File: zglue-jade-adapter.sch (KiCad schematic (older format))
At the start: 76 parts, among them J1 543630489, J2 543630489, U1 zGlue-Jade

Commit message: Update pinout and layout
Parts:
- removed TP28: TP_SMD1MM, antmicro-footprints:Testpoint_smd_1mm, symbol antmicroTestPoints:TP_SMD1MM
- added R29: R_0R_0402, antmicro-footprints:0402-res, symbol antmicroResistors0402:R_0R_0402
- added TP1: TP_SMD1MM, antmicro-footprints:Testpoint_smd_1mm, symbol antmicroTestPoints:TP_SMD1MM
- U1: symbol zglue-jade:zGlue-Jade -> zglue-jade-adapter-rescue:zGlue-Jade-zglue-jade
- renumbered TP1 to TP28
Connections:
- net labels added: PIO0, PIO13, PIO14
- net labels removed: PIO16, PIO17
- wire segments 277 -> 280
- no-connect marks 1 -> 14
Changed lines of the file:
@@
 	4200 4200 4800 4200
 Wire Wire Line
-	4200 4300 4800 4300
-Wire Wire Line
-	4200 4400 4800 4400
-Wire Wire Line
-	4200 4500 4800 4500
-Wire Wire Line
-	4200 4600 4800 4600
+	4200 4350 4800 4350
+Wire Wire Line
+	4200 4450 4800 4450
+Wire Wire Line
+	4200 4550 4800 4550
+Wire Wire Line
+	4200 4650 4800 4650
 Wire Wire Line
 	4200 4850 4800 4850
@@
 Text Label 4350 4200 0    50   ~ 0
 PROC_RST
-Text Label 4350 4300 0    50   ~ 0
+Text Label 1750 7050 0    50   ~ 0
 PROC_SI
-Text Label 4350 4400 0    50   ~ 0
+Text Label 1750 6950 0    50   ~ 0
 PROC_SO
-Text Label 4350 4500 0    50   ~ 0
+Text Label 1750 6750 0    50   ~ 0
 PROC_SCK
-Text Label 4350 4600 0    50   ~ 0
+Text Label 1750 6850 0    50   ~ 0
 PROC_SS
 Text Label 4350 4850 0    50   ~ 0
@@
 $EndComp
 $Comp
-L antmicroTestPoints:TP_SMD1MM TP1
+L antmicroTestPoints:TP_SMD1MM TP28
 U 1 1 5E08B0FD
 P 1650 5550
-F 0 "TP1" V 1650 5400 50  0000 C CNN
+F 0 "TP28" V 1650 5400 50  0000 C CNN
 F 1 "TP_SMD1MM" H 1650 5450 50  0001 C CNN
 F 2 "antmicro-footprints:Testpoint_smd_1mm" H 1850 5750 60  0001 L CNN
@@
 PIO15
 Wire Wire Line
-	2350 6950 1650 6950
+	2350 6950 1750 6950
 Wire Wire Line
 	2350 6750 1750 6750
 Wire Wire Line
 	2350 6850 1750 6850
-$Comp
-L antmicroTestPoints:TP_SMD1MM TP29
-U 1 1 5E0DD5A6
-P 1650 6850
-F 0 "TP29" V 1650 6700 50  0000 C CNN
-F 1 "TP_SMD1MM" H 1650 6750 50  0001 C CNN
-F 2 "antmicro-footprints:Testpoint_smd_1mm" H 1850 7050 60  0001 L CNN
-F 3 "" H 1850 7150 60  0001 L CNN
-	1    1650 6850
-	0    1    1    0
-$EndComp
-$Comp
-L antmicroTestPoints:TP_SMD1MM TP28
-U 1 1 5E0DD5AD
-P 1650 6750
-F 0 "TP28" V 1650 6600 50  0000 C CNN
-F 1 "TP_SMD1MM" H 1650 6650 50  0001 C CNN
-F 2 "antmicro-footprints:Testpoint_smd_1mm" H 1850 6950 60  0001 L CNN
-F 3 "" H 1850 7050 60  0001 L CNN
-	1    1650 6750
-	0    1    1    0
-$EndComp
-Text Label 1750 6850 0    50   ~ 0
-PIO17
-Text Label 1750 6750 0    50   ~ 0
-PIO16
-Wire Wire Line
-	2350 7050 1650 7050
-$Comp
-L zglue-jade:zGlue-Jade U1
+Text Label 1750 6550 0    50   ~ 0
+PIO14
+Text Label 1750 6450 0    50   ~ 0
+PIO13
+Wire Wire Line
+	2350 7050 1750 7050
+$Comp
+L zglue-jade-adapter-rescue:zGlue-Jade-zglue-jade U1
 U 1 1 5DB41B4F
 P 3200 3450
@@
 	0    1    1    0
 $EndComp
-Text Label 1750 6450 0    50   ~ 0
+Text Label 4350 4650 0    50   ~ 0
 PROC_INT
-Text Label 1750 6550 0    50   ~ 0
+Text Label 4350 4350 0    50   ~ 0
 CSI_INT
-Text Label 1650 6950 0    50   ~ 0
+Text Label 4350 4450 0    50   ~ 0
 LP_CSI_D1_OUT_P
-Text Label 1650 7050 0    50   ~ 0
+Text Label 4350 4550 0    50   ~ 0
 LP_CSI_D1_OUT_N
 Text Notes 6450 2600 0    50   ~ 0
 DNP
+NoConn ~ 8800 2550
+NoConn ~ 8800 2650
+NoConn ~ 8800 2850
+NoConn ~ 8800 2950
+NoConn ~ 9250 2950
+NoConn ~ 9250 3050
+NoConn ~ 12300 2250
+NoConn ~ 12300 2350
+NoConn ~ 12300 2550
+NoConn ~ 12300 2650
+NoConn ~ 12300 2850
+NoConn ~ 12300 2950
+NoConn ~ 12300 3150
+Wire Wire Line
+	2350 5150 1750 5150
+$Comp
+L antmicroTestPoints:TP_SMD1MM TP1
+U 1 1 5DF17D2C
+P 1650 5150
+F 0 "TP1" V 1650 5000 50  0000 C CNN
+F 1 "TP_SMD1MM" H 1650 5050 50  0001 C CNN
+F 2 "antmicro-footprints:Testpoint_smd_1mm" H 1850 5350 60  0001 L CNN
+F 3 "" H 1850 5450 60  0001 L CNN
+	1    1650 5150
+	0    1    1    0
+$EndComp
+Text Label 1750 5150 0    50   ~ 0
+PIO0
+Text Label 7900 4600 0    50   ~ 0
+PROC_RST
+$Comp
+L antmicroTestPoints:TP_SMD1MM TP29
+U 1 1 5DF566CE
+P 4900 4650
+F 0 "TP29" V 4900 4500 50  0000 C CNN
+F 1 "TP_SMD1MM" H 4900 4550 50  0001 C CNN
+F 2 "antmicro-footprints:Testpoint_smd_1mm" H 5100 4850 60  0001 L CNN
+F 3 "" H 5100 4950 60  0001 L CNN
+	1    4900 4650
+	0    -1   -1   0
+$EndComp
+$Comp
+L antmicroResistors0402:R_0R_0402 R29
+U 1 1 5DF56D0B
+P 8600 4600
+F 0 "R29" H 8800 4650 60  0000 C CNN
+F 1 "R_0R_0402" H 8600 4450 60  0001 C CNN
+F 2 "antmicro-footprints:0402-res" H 8800 4800 60  0001 L CNN
+F 3 "" H 8600 4600 50  0001 C CNN
+F 4 "PANASONIC" H 8800 5000 60  0001 L CNN "Manufacturer"
+F 5 "ERJ2GE0R00X" H 8800 4900 60  0001 L CNN "MPN"
+F 6 "0R" H 8950 4650 50  0000 C CNN "Val"
+	1    8600 4600
+	1    0    0    -1
+$EndComp
+Wire Wire Line
+	7900 4600 8450 4600
+Wire Wire Line
+	8750 4600 9700 4600
+Text Label 9100 4600 0    50   ~ 0
+E_PROC_RST
 $EndSCHEMATC

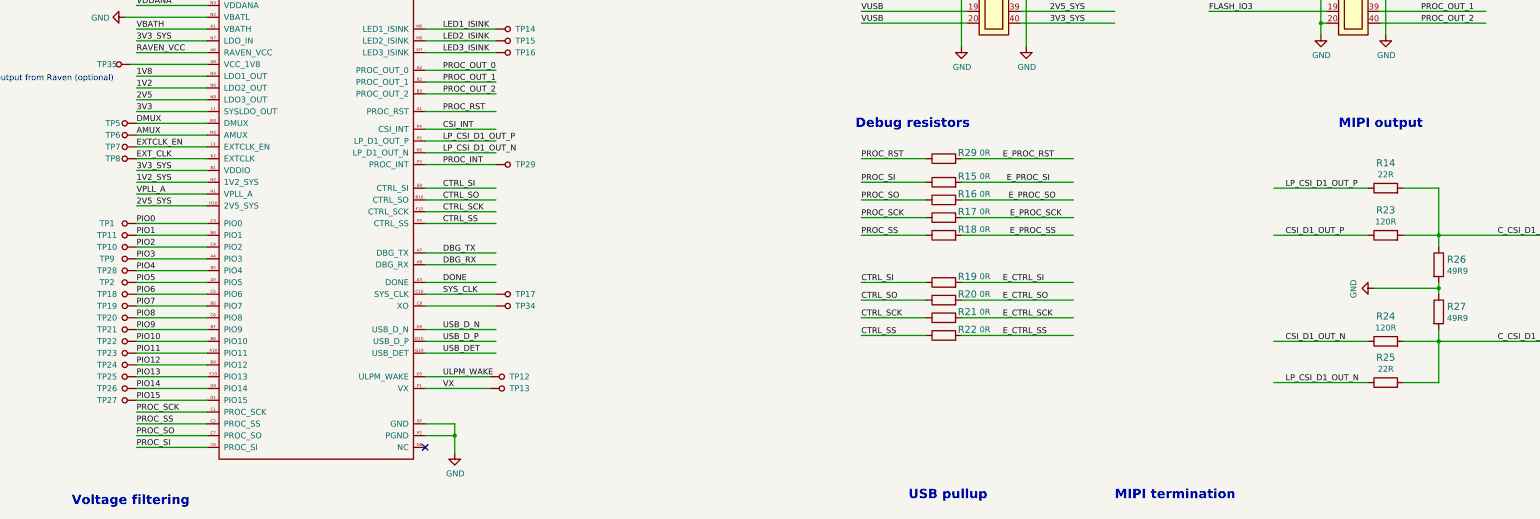
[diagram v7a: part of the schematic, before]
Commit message: Add resistors for choosing CSI_LP signals connection
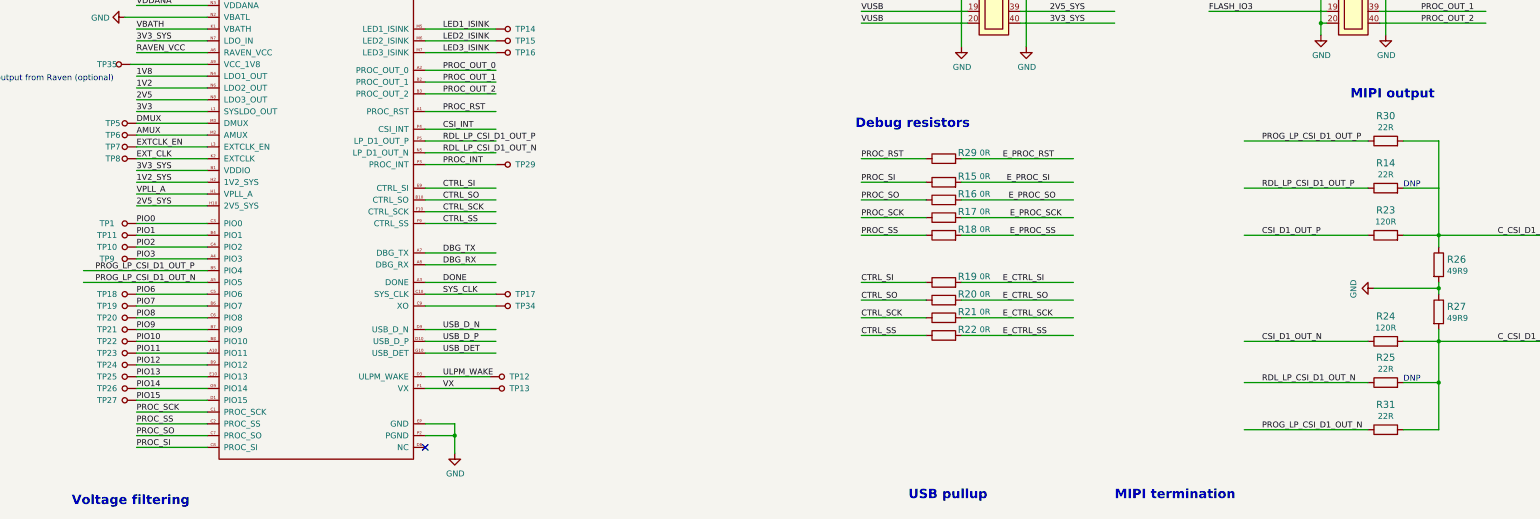
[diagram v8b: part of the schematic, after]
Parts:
- removed TP2, TP28: TP_SMD1MM, antmicro-footprints:Testpoint_smd_1mm, symbol antmicroTestPoints:TP_SMD1MM
- added R30, R31: R_22R_0402, antmicro-footprints:0402-res, symbol antmicroResistors0402:R_22R_0402
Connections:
- net labels added: PROG_LP_CSI_D1_OUT_N, PROG_LP_CSI_D1_OUT_P, RDL_LP_CSI_D1_OUT_N, RDL_LP_CSI_D1_OUT_P
- net labels removed: LP_CSI_D1_OUT_N, LP_CSI_D1_OUT_P, PIO4, PIO5
- wire segments 280 -> 286
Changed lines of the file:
@@
 	2350 5750 1750 5750
 Wire Wire Line
-	2350 5550 1750 5550
-Wire Wire Line
-	2350 5650 1750 5650
+	2350 5550 1300 5550
+Wire Wire Line
+	2350 5650 1300 5650
 $Comp
 L antmicroTestPoints:TP_SMD1MM TP18
@@
 	0    1    1    0
 $EndComp
-$Comp
-L antmicroTestPoints:TP_SMD1MM TP2
-U 1 1 5E08B0F6
-P 1650 5650
-F 0 "TP2" V 1650 5500 50  0000 C CNN
-F 1 "TP_SMD1MM" H 1650 5550 50  0001 C CNN
-F 2 "antmicro-footprints:Testpoint_smd_1mm" H 1850 5850 60  0001 L CNN
-F 3 "" H 1850 5950 60  0001 L CNN
-	1    1650 5650
-	0    1    1    0
-$EndComp
-$Comp
-L antmicroTestPoints:TP_SMD1MM TP28
-U 1 1 5E08B0FD
-P 1650 5550
-F 0 "TP28" V 1650 5400 50  0000 C CNN
-F 1 "TP_SMD1MM" H 1650 5450 50  0001 C CNN
-F 2 "antmicro-footprints:Testpoint_smd_1mm" H 1850 5750 60  0001 L CNN
-F 3 "" H 1850 5850 60  0001 L CNN
-	1    1650 5550
-	0    1    1    0
-$EndComp
 Text Label 1750 5750 0    50   ~ 0
 PIO6
-Text Label 1750 5650 0    50   ~ 0
-PIO5
-Text Label 1750 5550 0    50   ~ 0
-PIO4
 Wire Wire Line
 	2350 6050 1750 6050
@@
 $EndComp
 Wire Wire Line
-	12200 5250 11400 5250
-Wire Wire Line
-	12200 6150 11400 6150
+	12200 5250 11150 5250
+Wire Wire Line
+	12200 6150 11150 6150
 $Comp
 L antmicroResistors0402:R_49R9_0402 R26
@@
 Connection ~ 12800 6150
 Wire Wire Line
-	12200 6500 11400 6500
-Wire Wire Line
-	12200 4850 11400 4850
-Text Label 11500 4850 0    50   ~ 0
-LP_CSI_D1_OUT_P
-Text Label 11500 6500 0    50   ~ 0
-LP_CSI_D1_OUT_N
-Text Label 11500 5250 0    50   ~ 0
+	12200 6500 11150 6500
+Wire Wire Line
+	12200 4850 11150 4850
+Text Label 11300 4850 0    50   ~ 0
+RDL_LP_CSI_D1_OUT_P
+Text Label 11300 6500 0    50   ~ 0
+RDL_LP_CSI_D1_OUT_N
+Text Label 11300 5250 0    50   ~ 0
 CSI_D1_OUT_P
-Text Label 11500 6150 0    50   ~ 0
+Text Label 11300 6150 0    50   ~ 0
 CSI_D1_OUT_N
 Wire Wire Line
@@
 Text Label 13300 6150 0    50   ~ 0
 C_CSI_D1_OUT_N
-Text Notes 11950 4350 0    79   ~ 16
+Text Notes 12050 4100 0    79   ~ 16
 MIPI output
 Wire Wire Line
@@
 CSI_INT
 Text Label 4350 4450 0    50   ~ 0
-LP_CSI_D1_OUT_P
+RDL_LP_CSI_D1_OUT_P
 Text Label 4350 4550 0    50   ~ 0
-LP_CSI_D1_OUT_N
+RDL_LP_CSI_D1_OUT_N
 Text Notes 6450 2600 0    50   ~ 0
 DNP
@@
 Text Label 9100 4600 0    50   ~ 0
 E_PROC_RST
+Wire Wire Line
+	12800 6500 12800 6900
+Wire Wire Line
+	12800 6900 12500 6900
+Connection ~ 12800 6500
+$Comp
+L antmicroResistors0402:R_22R_0402 R31
+U 1 1 5DCA1BF5
+P 12350 6900
+F 0 "R31" H 12350 7113 60  0000 C CNN
+F 1 "R_22R_0402" H 12350 6750 60  0001 C CNN
+F 2 "antmicro-footprints:0402-res" H 12550 7100 60  0001 L CNN
+F 3 "" H 12350 6900 50  0001 C CNN
+F 4 "VISHAY" H 12550 7300 60  0001 L CNN "Manufacturer"
+F 5 "CRCW040222R0FKED" H 12550 7200 60  0001 L CNN "MPN"
+F 6 "22R" H 12350 7015 50  0000 C CNN "Val"
+	1    12350 6900
+	1    0    0    -1
+$EndComp
+Wire Wire Line
+	12200 6900 11150 6900
+Text Label 11300 6900 0    50   ~ 0
+PROG_LP_CSI_D1_OUT_N
+$Comp
+L antmicroResistors0402:R_22R_0402 R30
+U 1 1 5DD7B5FC
+P 12350 4450
+F 0 "R30" H 12350 4663 60  0000 C CNN
+F 1 "R_22R_0402" H 12350 4300 60  0001 C CNN
+F 2 "antmicro-footprints:0402-res" H 12550 4650 60  0001 L CNN
+F 3 "" H 12350 4450 50  0001 C CNN
+F 4 "VISHAY" H 12550 4850 60  0001 L CNN "Manufacturer"
+F 5 "CRCW040222R0FKED" H 12550 4750 60  0001 L CNN "MPN"
+F 6 "22R" H 12350 4565 50  0000 C CNN "Val"
+	1    12350 4450
+	1    0    0    -1
+$EndComp
+Wire Wire Line
+	12500 4450 12800 4450
+Wire Wire Line
+	12800 4450 12800 4850
+Wire Wire Line
+	12200 4450 11150 4450
+Text Label 11300 4450 0    50   ~ 0
+PROG_LP_CSI_D1_OUT_P
+Text Notes 12500 6500 0    50   ~ 0
+DNP
+Text Notes 12500 4850 0    50   ~ 0
+DNP
+Text Label 1400 5550 0    50   ~ 0
+PROG_LP_CSI_D1_OUT_P
+Text Label 1400 5650 0    50   ~ 0
+PROG_LP_CSI_D1_OUT_N
 $EndSCHEMATC
